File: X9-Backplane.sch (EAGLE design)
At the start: 8 parts

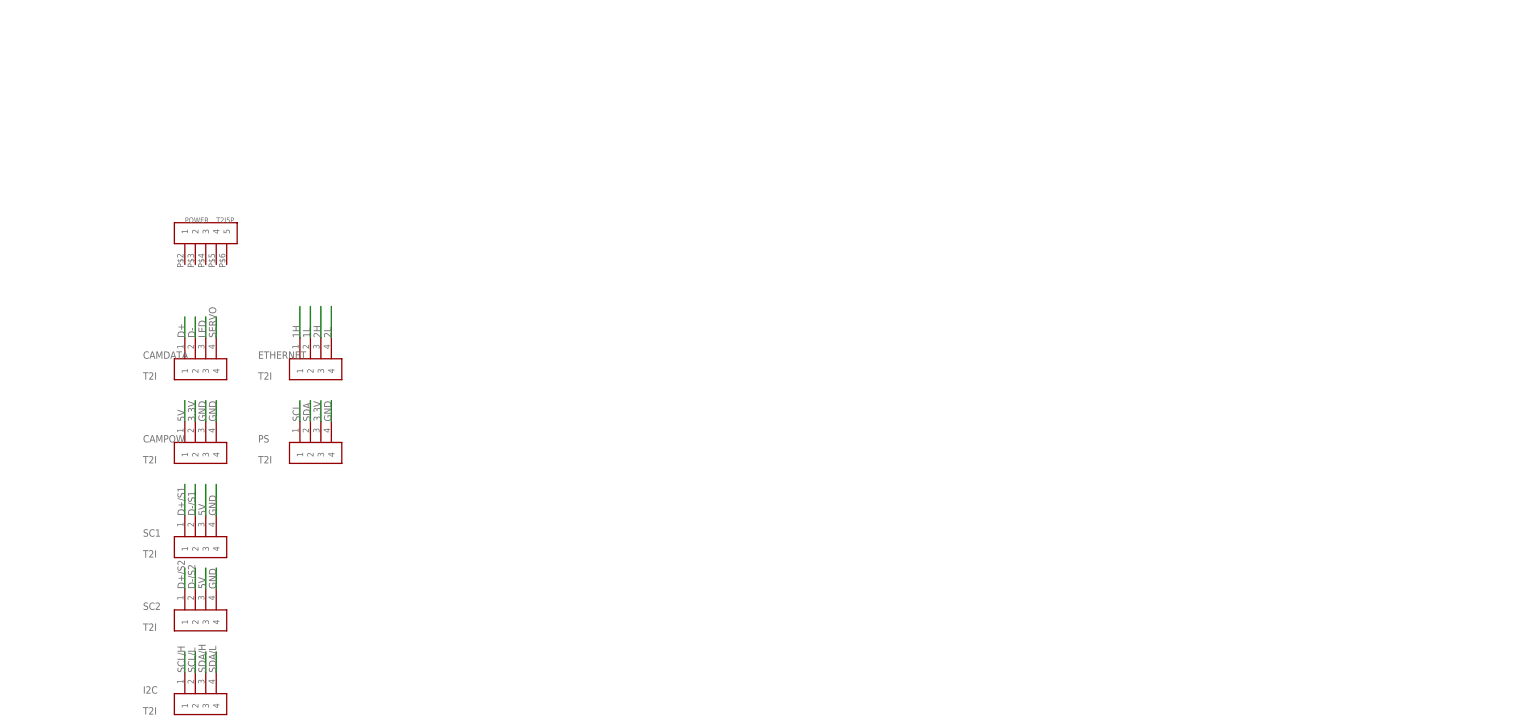
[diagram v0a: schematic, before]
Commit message: created the backplane
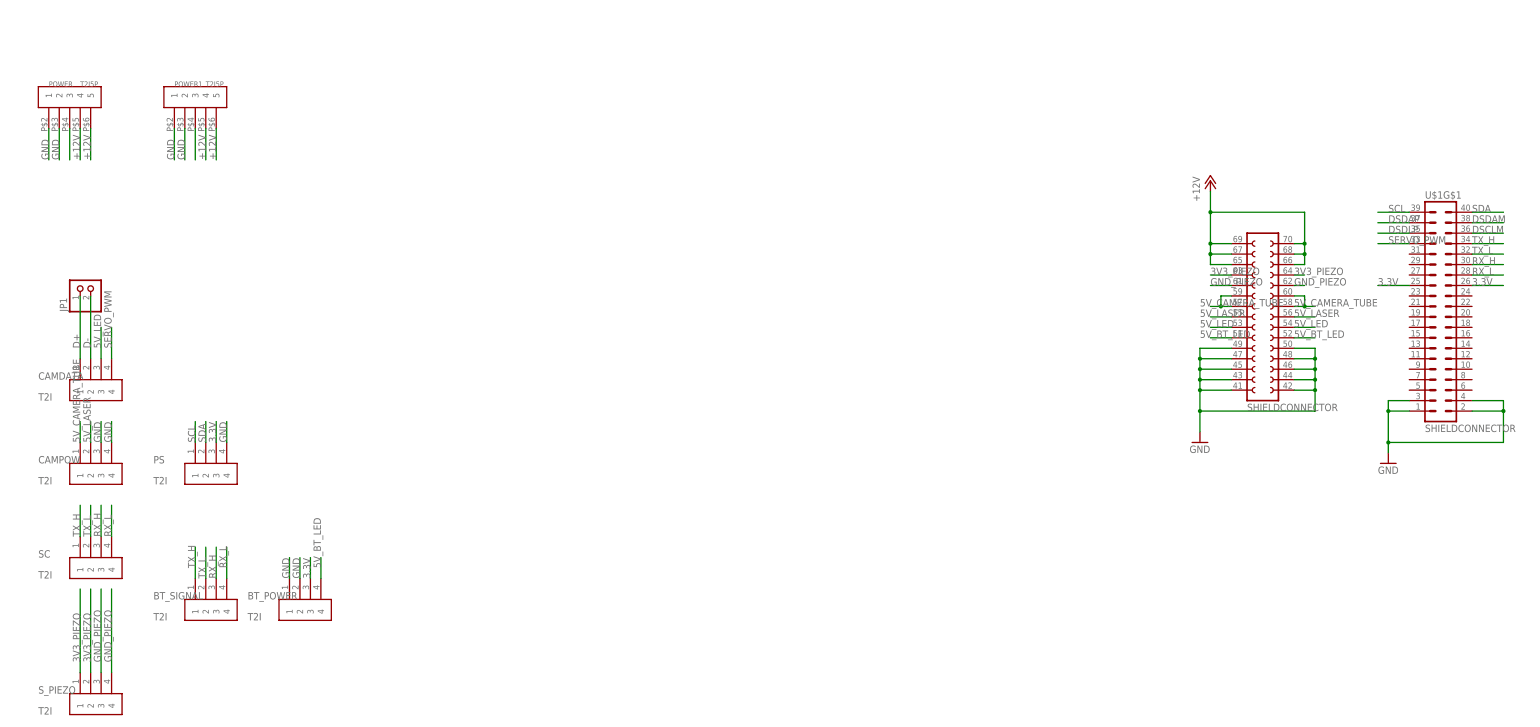
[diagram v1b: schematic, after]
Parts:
- removed ETHERNET, I2C, SC1, SC2: T2I, BACKPLANE:T2I
- added BT_POWER, BT_SIGNAL, SC, S_PIEZO: T2I, BACKPLANE:T2I
- added JP1: (no value), pinhead:PINHD-1X2
- added POWER1: T2I5P, T2I5P:T2I5P
- added U$1: SHIELDCONNECTOR, backplane_to_shield_connector:SHIELDCONNECTOR
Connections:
- removed net 1H: ETHERNET.1
- removed net 1L: ETHERNET.2
- removed net 2H: ETHERNET.3
- removed net 2L: ETHERNET.4
- removed net 5V: CAMPOW.1, SC1.3, SC2.3
- removed net D+/S1: SC1.1
- removed net D+/S2: SC2.1
- removed net D-/S1: SC1.2
- removed net D-/S2: SC2.2
- removed net LED: CAMDATA.3
- removed net SCL/H: I2C.1
- removed net SCL/L: I2C.2
- removed net SDA/H: I2C.3
- removed net SDA/L: I2C.4
- removed net SERVO: CAMDATA.4
- new net +12V: POWER.4, POWER.5, POWER1.4, POWER1.5, U$1G$2.12V@25, U$1G$2.12V@26, U$1G$2.12V@27, U$1G$2.12V@28, U$1G$2.12V@29, U$1G$2.12V@30
- new net 3V3_PIEZO: S_PIEZO.1, S_PIEZO.2, U$1G$2.3V3_PIEZO@23, U$1G$2.3V3_PIEZO@24
- new net 5V_BT_LED: BT_POWER.4, U$1G$2.5V_BT_LED@11, U$1G$2.5V_BT_LED@12
- new net 5V_CAMERA_TUBE: CAMPOW.1, U$1G$2.19, U$1G$2.20, U$1G$2.5V_CAMERA_TUBE@17, U$1G$2.5V_CAMERA_TUBE@18
- new net 5V_LASER: CAMPOW.2, U$1G$2.5V_LASER@15, U$1G$2.5V_LASER@16
- new net 5V_LED: CAMDATA.3, U$1G$2.5V_LED@13, U$1G$2.5V_LED@14
- new net DSCLM: U$1G$1.DSCLM@36
- new net DSDAM: U$1G$1.DSDAM@38
- new net DSDAP: U$1G$1.DSDAP@37
- new net DSDLP: U$1G$1.DSCLP@35
- new net GND_PIEZO: S_PIEZO.3, S_PIEZO.4, U$1G$2.GND_PIEZO@21, U$1G$2.GND_PIEZO@22
- new net N$23: POWER.3
- new net N$28: POWER1.3
- new net RX_H: BT_SIGNAL.3, SC.3, U$1G$1.Z@30
- new net RX_L: BT_SIGNAL.4, SC.4, U$1G$1.Y@28
- new net SERVO_PWM: CAMDATA.4, U$1G$1.SERVO_PWM@33
- new net TX_H: BT_SIGNAL.1, SC.1, U$1G$1.A@34
- new net TX_L: BT_SIGNAL.2, SC.2, U$1G$1.B@32
- net 3.3V: now also BT_POWER.3, U$1G$1.25, U$1G$1.26; no longer CAMPOW.2
- net D+: now also JP1.1
- net D-: now also JP1.2
- net GND: now also BT_POWER.1, BT_POWER.2, POWER.1, POWER.2, POWER1.1, POWER1.2, U$1G$1.1, U$1G$1.2, U$1G$1.3, U$1G$1.4, U$1G$2.GND@1, U$1G$2.GND@10, U$1G$2.GND@2, U$1G$2.GND@3, U$1G$2.GND@4, U$1G$2.GND@5, U$1G$2.GND@6, U$1G$2.GND@7, U$1G$2.GND@8, U$1G$2.GND@9; no longer SC1.4, SC2.4
- net SCL: now also U$1G$1.SCL@39
- net SDA: now also U$1G$1.SDA@40
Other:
- moved on the sheet: CAMDATA, CAMPOW, POWER, PS

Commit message: Modified BT and PS
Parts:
- PS: value T2I -> DF13-4P-1.25DSA; device BACKPLANE:T2I -> con-hirose-df13:DF13-4P-1.25DSA
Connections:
- removed net DSCLM: U$1G$1.DSCLM@36
- removed net DSDAM: U$1G$1.DSDAM@38
- removed net DSDAP: U$1G$1.DSDAP@37
- removed net DSDLP: U$1G$1.DSCLP@35
- removed net N$23: POWER.3
- removed net N$28: POWER1.3
- new net RX_BT: BT_SIGNAL.2, U$1G$1.22
- new net TX_BT: BT_SIGNAL.1, U$1G$1.20
- net 3.3V: now also BT_SIGNAL.4, PS.1; no longer BT_POWER.3, PS.3
- net 5V_BT_LED: now also BT_POWER.3
- net GND: now also BT_SIGNAL.3
- net RX_H: no longer BT_SIGNAL.3
- net RX_L: no longer BT_SIGNAL.4
- net SCL: now also PS.2; no longer PS.1
- net SDA: now also PS.3; no longer PS.2
- net TX_H: no longer BT_SIGNAL.1
- net TX_L: no longer BT_SIGNAL.2
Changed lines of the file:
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@@
 <part name="SC" library="BACKPLANE" deviceset="T2I" device=""/>
 <part name="S_PIEZO" library="BACKPLANE" deviceset="T2I" device=""/>
-<part name="PS" library="BACKPLANE" deviceset="T2I" device=""/>
 <part name="POWER1" library="T2I5P" deviceset="T2I5P" device=""/>
 <part name="BT_SIGNAL" library="BACKPLANE" deviceset="T2I" device=""/>
@@
 <part name="JP1" library="pinhead" deviceset="PINHD-1X2" device=""/>
 <part name="GND2" library="supply1" deviceset="GND" device=""/>
+<part name="PS" library="con-hirose-df13" deviceset="DF13-4P-1.25" device="DSA"/>
 </parts>
 <sheets>
@@
 <instance part="SC" gate="G$1" x="33.02" y="71.12"/>
 <instance part="S_PIEZO" gate="G$1" x="33.02" y="38.1"/>
-<instance part="PS" gate="G$1" x="60.96" y="93.98"/>
 <instance part="POWER1" gate="&gt;NAME" x="63.5" y="187.96"/>
 <instance part="BT_SIGNAL" gate="G$1" x="60.96" y="60.96"/>
@@
 <instance part="JP1" gate="G$1" x="38.1" y="144.78" rot="R90"/>
 <instance part="GND2" gate="1" x="353.06" y="101.6"/>
+<instance part="PS" gate="G$1" x="71.12" y="116.84" smashed="yes" rot="R270">
+<attribute name="NAME" x="76.2" y="118.745" size="1.778" layer="95" rot="R270"/>
+<attribute name="VALUE" x="61.9125" y="118.745" size="1.778" layer="96" rot="R270"/>
+</instance>
 </instances>
 <busses>
@@
 <net name="3.3V" class="0">
 <segment>
-<pinref part="PS" gate="G$1" pin="3"/>
-<wire x1="68.58" y1="106.68" x2="68.58" y2="111.76" width="0.1524" layer="91"/>
-<label x="68.58" y="106.68" size="1.778" layer="95" rot="R90"/>
-</segment>
-<segment>
-<pinref part="BT_POWER" gate="G$1" pin="3"/>
-<wire x1="91.44" y1="73.66" x2="91.44" y2="78.74" width="0.1524" layer="91"/>
-<label x="91.44" y="73.66" size="1.778" layer="95" rot="R90"/>
-</segment>
-<segment>
 <pinref part="U$1" gate="G$1" pin="25"/>
 <wire x1="358.14" y1="144.78" x2="350.52" y2="144.78" width="0.1524" layer="91"/>
@@
 <label x="373.38" y="144.78" size="1.778" layer="95"/>
 </segment>
+<segment>
+<pinref part="PS" gate="G$1" pin="1"/>
+<wire x1="73.66" y1="121.92" x2="73.66" y2="127" width="0.1524" layer="91"/>
+<label x="73.66" y="129.54" size="1.778" layer="95" rot="R270"/>
+</segment>
+<segment>
+<pinref part="BT_SIGNAL" gate="G$1" pin="4"/>
+<wire x1="71.12" y1="73.66" x2="71.12" y2="81.28" width="0.1524" layer="91"/>
+<label x="71.12" y="76.2" size="1.778" layer="95" rot="R90"/>
+</segment>
 </net>
 <net name="GND" class="0">
@@
 <wire x1="43.18" y1="106.68" x2="43.18" y2="111.76" width="0.1524" layer="91"/>
 <label x="43.18" y="106.68" size="1.778" layer="95" rot="R90"/>
-</segment>
-<segment>
-<pinref part="PS" gate="G$1" pin="4"/>
-<wire x1="71.12" y1="106.68" x2="71.12" y2="111.76" width="0.1524" layer="91"/>
-<label x="71.12" y="106.68" size="1.778" layer="95" rot="R90"/>
 </segment>
 <segment>
@@
 <pinref part="GND2" gate="1" pin="GND"/>
 </segment>
+<segment>
+<pinref part="PS" gate="G$1" pin="4"/>
+<wire x1="66.04" y1="121.92" x2="66.04" y2="127" width="0.1524" layer="91"/>
+<label x="66.04" y="129.54" size="1.778" layer="95" rot="R270"/>
+</segment>
+<segment>
+<pinref part="BT_SIGNAL" gate="G$1" pin="3"/>
+<wire x1="68.58" y1="73.66" x2="68.58" y2="81.28" width="0.1524" layer="91"/>
+<label x="68.58" y="73.66" size="1.778" layer="95" rot="R90"/>
+</segment>
 </net>
 <net name="TX_H" class="0">
@@
 </segment>
 <segment>
-<pinref part="BT_SIGNAL" gate="G$1" pin="1"/>
-<wire x1="63.5" y1="73.66" x2="63.5" y2="81.28" width="0.1524" layer="91"/>
-<label x="63.5" y="76.2" size="1.778" layer="95" rot="R90"/>
-</segment>
-<segment>
 <pinref part="U$1" gate="G$1" pin="A@34"/>
 <wire x1="373.38" y1="154.94" x2="381" y2="154.94" width="0.1524" layer="91"/>
@@
 </segment>
 <segment>
-<pinref part="BT_SIGNAL" gate="G$1" pin="2"/>
-<wire x1="66.04" y1="73.66" x2="66.04" y2="81.28" width="0.1524" layer="91"/>
-<label x="66.04" y="73.66" size="1.778" layer="95" rot="R90"/>
-</segment>
-<segment>
 <pinref part="U$1" gate="G$1" pin="B@32"/>
 <wire x1="373.38" y1="152.4" x2="381" y2="152.4" width="0.1524" layer="91"/>
@@
 <net name="SCL" class="0">
 <segment>
-<pinref part="PS" gate="G$1" pin="1"/>
-<wire x1="63.5" y1="106.68" x2="63.5" y2="111.76" width="0.1524" layer="91"/>
-<label x="63.5" y="106.68" size="1.778" layer="95" rot="R90"/>
-</segment>
-<segment>
 <pinref part="U$1" gate="G$1" pin="SCL@39"/>
 <wire x1="358.14" y1="162.56" x2="350.52" y2="162.56" width="0.1524" layer="91"/>
 <label x="353.06" y="162.56" size="1.778" layer="95"/>
 </segment>
+<segment>
+<pinref part="PS" gate="G$1" pin="2"/>
+<wire x1="71.12" y1="121.92" x2="71.12" y2="127" width="0.1524" layer="91"/>
+<label x="71.12" y="129.54" size="1.778" layer="95" rot="R270"/>
+</segment>
 </net>
 <net name="SDA" class="0">
-<segment>
-<pinref part="PS" gate="G$1" pin="2"/>
-<wire x1="66.04" y1="106.68" x2="66.04" y2="111.76" width="0.1524" layer="91"/>
-<label x="66.04" y="106.68" size="1.778" layer="95" rot="R90"/>
-</segment>
 <segment>
 <pinref part="U$1" gate="G$1" pin="SDA@40"/>
@@
 <label x="373.38" y="162.56" size="1.778" layer="95"/>
 </segment>
+<segment>
+<pinref part="PS" gate="G$1" pin="3"/>
+<wire x1="68.58" y1="121.92" x2="68.58" y2="127" width="0.1524" layer="91"/>
+<label x="68.58" y="129.54" size="1.778" layer="95" rot="R270"/>
+</segment>
 </net>
 <net name="5V_LASER" class="0">
@@
 </segment>
 </net>
-<net name="N$23" class="0">
-<segment>
-<pinref part="POWER" gate="&gt;NAME" pin="3"/>
-<wire x1="33.02" y1="182.88" x2="33.02" y2="175.26" width="0.1524" layer="91"/>
-</segment>
-</net>
-<net name="N$28" class="0">
-<segment>
-<pinref part="POWER1" gate="&gt;NAME" pin="3"/>
-<wire x1="63.5" y1="182.88" x2="63.5" y2="175.26" width="0.1524" layer="91"/>
-</segment>
-</net>
 <net name="RX_H" class="0">
 <segment>
@@
 </segment>
 <segment>
-<pinref part="BT_SIGNAL" gate="G$1" pin="3"/>
-<wire x1="68.58" y1="73.66" x2="68.58" y2="81.28" width="0.1524" layer="91"/>
-<label x="68.58" y="73.66" size="1.778" layer="95" rot="R90"/>
-</segment>
-<segment>
 <pinref part="U$1" gate="G$1" pin="Z@30"/>
 <wire x1="373.38" y1="149.86" x2="381" y2="149.86" width="0.1524" layer="91"/>
@@
 </segment>
 <segment>
-<pinref part="BT_SIGNAL" gate="G$1" pin="4"/>
-<wire x1="71.12" y1="73.66" x2="71.12" y2="81.28" width="0.1524" layer="91"/>
-<label x="71.12" y="76.2" size="1.778" layer="95" rot="R90"/>
-</segment>
-<segment>
 <pinref part="U$1" gate="G$1" pin="Y@28"/>
 <wire x1="373.38" y1="147.32" x2="381" y2="147.32" width="0.1524" layer="91"/>
@@
 </segment>
 </net>
-<net name="DSDAP" class="0">
-<segment>
-<pinref part="U$1" gate="G$1" pin="DSDAP@37"/>
-<wire x1="358.14" y1="160.02" x2="350.52" y2="160.02" width="0.1524" layer="91"/>
-<label x="353.06" y="160.02" size="1.778" layer="95"/>
-</segment>
-</net>
-<net name="DSDLP" class="0">
-<segment>
-<pinref part="U$1" gate="G$1" pin="DSCLP@35"/>
-<wire x1="358.14" y1="157.48" x2="350.52" y2="157.48" width="0.1524" layer="91"/>
-<label x="353.06" y="157.48" size="1.778" layer="95"/>
-</segment>
-</net>
 <net name="SERVO_PWM" class="0">
 <segment>
@@
 <wire x1="43.18" y1="127" x2="43.18" y2="134.62" width="0.1524" layer="91"/>
 <label x="43.18" y="129.54" size="1.778" layer="95" rot="R90"/>
-</segment>
-</net>
-<net name="DSDAM" class="0">
-<segment>
-<pinref part="U$1" gate="G$1" pin="DSDAM@38"/>
-<wire x1="373.38" y1="160.02" x2="381" y2="160.02" width="0.1524" layer="91"/>
-<label x="373.38" y="160.02" size="1.778" layer="95"/>
-</segment>
-</net>
-<net name="DSCLM" class="0">
-<segment>
-<pinref part="U$1" gate="G$1" pin="DSCLM@36"/>
-<wire x1="373.38" y1="157.48" x2="381" y2="157.48" width="0.1524" layer="91"/>
-<label x="373.38" y="157.48" size="1.778" layer="95"/>
 </segment>
 </net>
@@
 <label x="93.98" y="76.2" size="1.778" layer="95" rot="R90"/>
 </segment>
-</net>
+<segment>
+<pinref part="BT_POWER" gate="G$1" pin="3"/>
+<wire x1="91.44" y1="73.66" x2="91.44" y2="78.74" width="0.1524" layer="91"/>
+<label x="91.44" y="73.66" size="1.778" layer="95" rot="R90"/>
+</segment>
+</net>
+<net name="RX_BT" class="0">
+<segment>
+<pinref part="U$1" gate="G$1" pin="22"/>
+<wire x1="373.38" y1="139.7" x2="381" y2="139.7" width="0.1524" layer="91"/>
+<label x="373.38" y="139.7" size="1.778" layer="95"/>
+</segment>
+<segment>
+<pinref part="BT_SIGNAL" gate="G$1" pin="2"/>
+<wire x1="66.04" y1="73.66" x2="66.04" y2="81.28" width="0.1524" layer="91"/>
+<label x="66.04" y="73.66" size="1.778" layer="95" rot="R90"/>
+</segment>
+</net>
+<net name="TX_BT" class="0">
+<segment>
+<pinref part="U$1" gate="G$1" pin="20"/>
+<wire x1="373.38" y1="137.16" x2="381" y2="137.16" width="0.1524" layer="91"/>
+<label x="373.38" y="137.16" size="1.778" layer="95"/>
+</segment>
+<segment>
+<pinref part="BT_SIGNAL" gate="G$1" pin="1"/>
+<wire x1="63.5" y1="73.66" x2="63.5" y2="81.28" width="0.1524" layer="91"/>
+<label x="63.5" y="76.2" size="1.778" layer="95" rot="R90"/>
+</segment>
+</net>
